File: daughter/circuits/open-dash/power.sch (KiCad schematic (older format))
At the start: 46 parts, among them J10 Barrel_Jack_OD5.5_ID2.5, J11 Barrel_Jack_OD5.5_ID2.5, J9 Barrel_Jack_OD5.5_ID2.5, U1 Opto_TLP521, U11 REG_AMS1117-3.3, U2 ACS711, U4 MIC29302WU, U5 MIC29302WU, U6 MIC29302WU

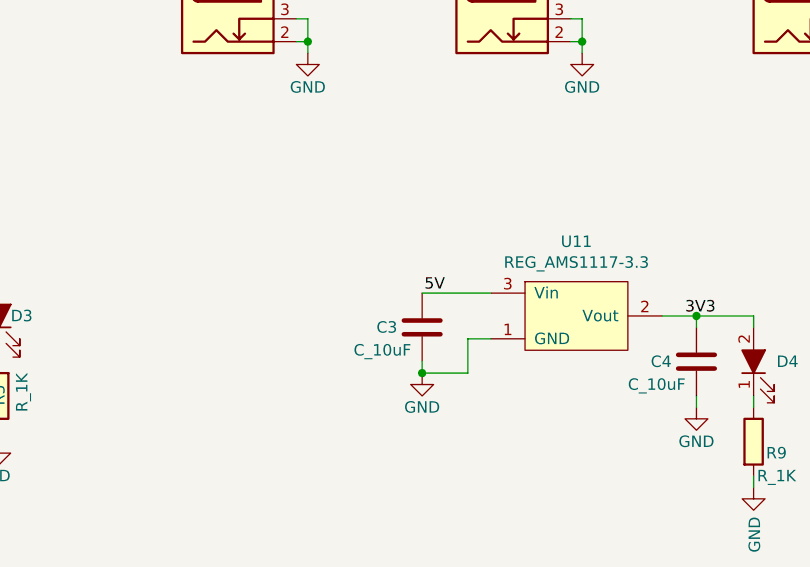
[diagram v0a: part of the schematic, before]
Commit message: send v1.4 to board house. Corrected source-drain on fets.
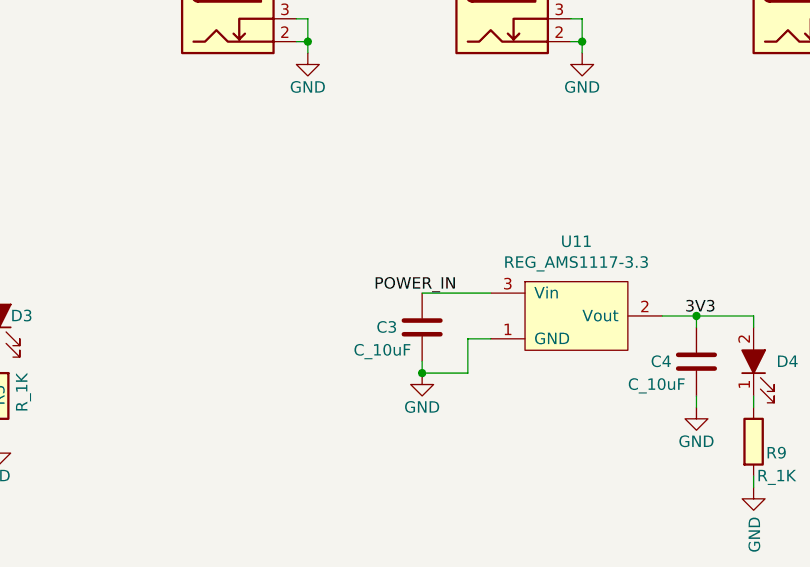
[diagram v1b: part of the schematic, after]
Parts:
- U11: LCSC C6186 -> C347222
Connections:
- net 5V: no longer C3.1, U11.3 (Vin)
- net BATTERY: now also C3.1, U11.3 (Vin)
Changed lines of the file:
@@
 	1    0    0    -1
 $EndComp
-Text Label 4400 2950 2    50   ~ 0
-5V
 Wire Wire Line
 	4300 3250 4300 3300
@@
 	5350 3050 5500 3050
 Connection ~ 5500 3050
-$Comp
-L Open_Automation:REG_AMS1117-3.3 U11
-U 1 1 607097AC
-P 5000 3050
-F 0 "U11" H 4975 3375 50  0000 C CNN
-F 1 "REG_AMS1117-3.3" H 4975 3284 50  0000 C CNN
-F 2 "Package_TO_SOT_SMD:SOT-223-3_TabPin2" H 4950 2775 50  0001 C CIN
-F 3 "https://datasheet.lcsc.com/szlcsc/1811201117_Advanced-Monolithic-Systems-AMS-AMS1117-3-3_C6186.pdf" H 4975 2700 50  0001 C CNN
-F 4 "AMS1117-3.3" H 5025 3375 60  0001 C CNN "Part Number"
-F 5 "C6186" H 4950 3450 50  0001 C CNN "LCSC"
-	1    5000 3050
-	1    0    0    -1
-$EndComp
 $Comp
 L Open_Automation:R_100K_0402 R3
@@
 Text HLabel 1700 1700 0    60   Input ~ 0
 5V_EN
+$Comp
+L Open_Automation:REG_AMS1117-3.3 U11
+U 1 1 61F30C06
+P 5000 3050
+F 0 "U11" H 4975 3375 50  0000 C CNN
+F 1 "REG_AMS1117-3.3" H 4975 3284 50  0000 C CNN
+F 2 "Package_TO_SOT_SMD:SOT-223-3_TabPin2" H 4950 2775 50  0001 C CIN
+F 3 "https://datasheet.lcsc.com/szlcsc/1811201117_Advanced-Monolithic-Systems-AMS-AMS1117-3-3_C6186.pdf" H 4975 2700 50  0001 C CNN
+F 4 "AMS1117-3.3" H 5025 3375 60  0001 C CNN "Part Number"
+F 5 "C347222" H 4950 3450 50  0001 C CNN "LCSC"
+	1    5000 3050
+	1    0    0    -1
+$EndComp
+Text Label 4450 2950 2    50   ~ 0
+POWER_IN
 $EndSCHEMATC
